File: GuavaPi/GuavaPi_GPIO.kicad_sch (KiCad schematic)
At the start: 1 part

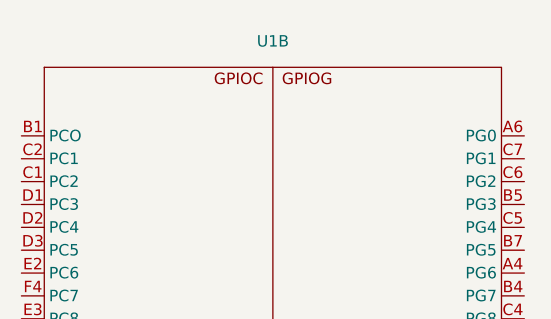
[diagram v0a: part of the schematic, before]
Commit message: Started DRAM Design
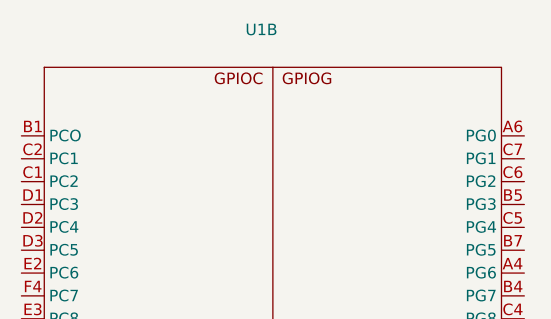
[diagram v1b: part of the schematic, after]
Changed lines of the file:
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@@
   (symbol (lib_id "Allwinner_H616:Allwinner_H616") (at 14.1224 20.828 0) (unit 2)
     (in_bom yes) (on_board yes) (dnp no) (fields_autoplaced)
-    (property "Reference" "U1" (at 52.2224 24.2824 0)
+    (property "Reference" "U1" (at 50.9524 23.0124 0)
       (effects (font (size 1.27 1.27)))
     )
@@
           (reference "U1") (unit 2)
         )
+        (path "/3be7235b-2d12-456d-bbdb-dcc9c2ae1afd/dc1a4d83-a933-4336-ba01-88286996a5dc"
+          (reference "U1") (unit 2)
+        )

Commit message: Added EEMC
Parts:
- added C68, C69, C70, C71, C72, C73: 2u2, symbol Device:C
- added R16, R17: 47k, symbol Device:R
- added U2: EMMC04G-M627-A01, BGA153C50P14X14_1300X1150X100, symbol EMMC04G-M627-A01:EMMC04G-M627-A01
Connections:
- new net: C72.1, C73.1, U2.C2 (VDDI)
- new net +3.3V: C68.2, C69.2, C70.2, C71.2, R16.2, R17.2, U2.C6 (VCCQ), U2.E6 (VCC), U2.F5 (VCC), U2.J10 (VCC), U2.K9 (VCC), U2.M4 (VCCQ), U2.N4 (VCCQ), U2.P3 (VCCQ), U2.P5 (VCCQ)
- new net GND: C68.1, C69.1, C70.1, C71.1, C72.2, C73.2, U2.A6 (VSS), U2.C4 (VSSQ), U2.E7 (VSS), U2.G5 (VSS), U2.H10 (VSS), U2.J5 (VSS), U2.K8 (VSS), U2.N2 (VSSQ), U2.N5 (VSSQ), U2.P4 (VSSQ), U2.P6 (VSSQ)
- new net SDC2_CLK: U2.M6 (CLK)
- new net SDC2_CMD: R16.1, U2.M5 (CMD)
- new net SDC2_D0: U2.A3 (DAT0)
- new net SDC2_D1: U2.A4 (DAT1)
- new net SDC2_D2: U2.A5 (DAT2)
- new net SDC2_D3: U2.B2 (DAT3)
- new net SDC2_D4: U2.B3 (DAT4)
- new net SDC2_D5: U2.B4 (DAT5)
- new net SDC2_D6: U2.B5 (DAT6)
- new net SDC2_D7: U2.B6 (DAT7)
- new net SDC2_DS: R17.1, U2.H5 (DS)
- new net SDC2_RST: U2.K5 (RST_N)

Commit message: WIFI + BT Connections
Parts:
- added A1: RFECA3216060A1T_NEW3_M, picoclick_c3_v1.1:RFECA3216060A1T_NEW3_M, symbol picoclick_c3_v1.1-eagle-import:RFECA3216060A1T_NEW3_M
- added ANT1: 211964-0001, 2119640001:2119640001, symbol 211964-0001:211964-0001
- added B1: BUTTON_4PIN, picoclick_c3_v1.1:BUTTON_SMD_12MM, symbol picoclick_c3_v1.1-eagle-import:BUTTON_4PIN
- added C74, C75: C, symbol Device:C
- added C76: 0.1uF, symbol Device:C
- added C77: 10uF, symbol Device:C
- added C78: 10µ, picoclick_c3_v1.1:C0402_S, symbol picoclick_c3_v1.1-eagle-import:C0402_S
- added C79, C87: 0,1µ, picoclick_c3_v1.1:C0402_S, symbol picoclick_c3_v1.1-eagle-import:C0402_S
- added C80: 2.2uF, symbol Device:C
- added C81, C82: C-EU-0402-WOKEEPOUT_S, picoclick_c3_v1.1:C0402_S, symbol picoclick_c3_v1.1-eagle-import:C-EU-0402-WOKEEPOUT_S
- added C83, C88, C93: 1µ, picoclick_c3_v1.1:C0402_S, symbol picoclick_c3_v1.1-eagle-import:C0402_S
- added C84, C85: 10p, picoclick_c3_v1.1:C0402_S, symbol picoclick_c3_v1.1-eagle-import:C0402_S
- added C86: NC, symbol Device:C
- added C89: C0402_S, picoclick_c3_v1.1:C0402_S, symbol picoclick_c3_v1.1-eagle-import:C0402_S
- added C90: 3.3pF, picoclick_c3_v1.1:C0402_S, symbol picoclick_c3_v1.1-eagle-import:C0402_S
- added C92: 1nH, picoclick_c3_v1.1:C0402_S, symbol picoclick_c3_v1.1-eagle-import:C0402_S
- added D3: DAN222, picoclick_c3_v1.1:SOT523, symbol picoclick_c3_v1.1-eagle-import:DAN222
- added J2: SMT_JUMPER_2_NC_PASTE, picoclick_c3_v1.1:JUMPER_SMALL, symbol picoclick_c3_v1.1-eagle-import:SMT_JUMPER_2_NC_PASTE
- added J4: JUMPER_SMALL, picoclick_c3_v1.1:JUMPER_SMALL, symbol picoclick_c3_v1.1-eagle-import:JUMPER_SMALL
- added R18, R19: R, symbol Device:R
- added R20, R22, R26, R31, R33: 100k, symbol Device:R
- added R21: 0R, symbol Device:R
- added R23: 1k, picoclick_c3_v1.1:R0402, symbol picoclick_c3_v1.1-eagle-import:R0402
- added R24, R25, R28, R29, R30: 10k, picoclick_c3_v1.1:R0402, symbol picoclick_c3_v1.1-eagle-import:R0402
- added R27: 1M, picoclick_c3_v1.1:R0402, symbol picoclick_c3_v1.1-eagle-import:R0402
- added R32, R37, R38, R39, R41, R42: 47k, symbol Device:R
- added R35, R36: 5.1k, picoclick_c3_v1.1:R0402, symbol picoclick_c3_v1.1-eagle-import:R0402
- added U3: ~, symbol Allwinner_H616:6223A-SRD
- added U6: ESP32_C3_QFN32, picoclick_c3_v1.1:QFN32, symbol picoclick_c3_v1.1-eagle-import:ESP32_C3_QFN32
- added U7: MIC5504, picoclick_c3_v1.1:TDFN4, symbol picoclick_c3_v1.1-eagle-import:MIC5504
- added U9: USB_C_C393939, picoclick_c3_v1.1:USBC_C393939, symbol picoclick_c3_v1.1-eagle-import:USB_C_C393939
- added X1: CM9V_T1A, picoclick_c3_v1.1:XTAL_1016, symbol picoclick_c3_v1.1-eagle-import:CM9V_T1A
- added X2: XTAL_2016, picoclick_c3_v1.1:XTAL_2016, symbol picoclick_c3_v1.1-eagle-import:XTAL_2016
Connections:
- net +3.3V: now also R22.2, R32.2
- net GND: now also A1.PGND1 (GND), A1.PGND2 (GND), ANT1.2 (FEED), C74.2, C75.2, C76.2, C77.2, C78.P$1 (1), C79.P$1 (1), C80.1, C81.P$2 (2), C82.P$2 (2), C83.P$1 (1), C84.P$1 (1), C85.P$1 (1), C86.2, C87.P$1 (1), C88.P$1 (1), C89.P$2 (2), C92.P$2 (2), C93.P$1 (1), J2.P$1 (1), R20.1, R24.2, R25.1, R26.2, R27.1, R35.2, R36.2, U3.1 (AGND), U3.20 (AGND), U3.3 (AGND), U3.31 (AGND), U3.33 (AGND), U3.36 (AGND), U6.EXP, U7.EXP (GND), U7.P2 (GND), U9.A1B12 (GND), U9.B1A12 (GND), U9.S1 (SHLD), U9.S2 (SHLD), U9.S3 (SHLD), U9.S4 (SHLD), X2.P2 (G), X2.P4 (G)
- new net: R36.1, U9.B5 (CC2)
- new net: ANT1.1 (GROUND), C75.1, R18.1, R19.1
- new net: C74.1, R18.2, U3.2 (WL_BT_ANT)
- new net: R22.1, U3.34 (BT_DIS#)
- new net: A1.PFEED (ANT), C89.P$1 (1), C90.P$1 (1)
- new net: B1.P2 (2), R23.2
- new net: C76.1, C77.1, R21.2, U3.9 (VBAT_IN)
- new net: R32.1, U3.24 (SUSCLK_IN)
- new net: R35.1, U9.A5 (CC1)
- new net: C84.P$2 (2), U6.30 (XTAL_P), X2.P1 (1)
- new net: C85.P$2 (2), U6.29 (XTAL_N), X2.P3 (2)
- new net: R20.2, U3.6 (HOST_WAKE_BT)
- new net: R31.1, U3.30 (MAIN_XTAL_IN)
- new net +3V3: C78.P$2 (2), C79.P$2 (2), C87.P$2 (2), C93.P$2 (2), R28.1, R29.1, R30.1, U6.11 (VDD3P3_RTC), U6.17 (VDD3P3_CPU), U6.2 (VDD3P3), U6.3 (VDD3P3_1), U6.31 (VDDA), U6.32 (VDDA_1), U7.P1 (VOUT)
- new net +VBAT: B1.P4 (4), C88.P$2 (2), J4.P$1 (1), U7.P4 (VIN)
- new net +VUSB: J4.P$2 (2), U9.A4B9 (VBUS), U9.B4A9 (VBUS)
- new net ADC: U6.9 (MTMS)
- new net AP-CLK24M-OUT: R31.2
- new net AP-SDC1-01: R42.1, U3.19 (SD_D1)
- new net AP-SDC1-CLK: C86.1, U3.17 (SD_CLK)
- new net AP-SDC1-CMD: R39.1, U3.16 (SD_CMD)
- new net AP-SDC1-D0: R41.1, U3.18 (SD_D0)
- new net AP-SDC1-D2: R37.1, U3.14 (SD_D2)
- new net AP-SDC1-D3: R38.1, U3.15 (SD_D3)
- new net AP-UART1-CTS: R26.1, U3.41 (UART_RTS)
- new net AP-UART1-RTS: U3.44 (UART_CTS)
- new net AP-UART1-RX: U3.42 (UART_OUT)
- new net AP-UART1-TX: U3.43 (UART_IN)
- new net BUTTON: C83.P$2 (2), D3.2, R23.1, R24.1, U6.10 (MTDI)
- new net DATA-Ready: U6.19 (SPIHD)
- new net EN: R30.2, U6.7 (CHIP_EN)
- new net EN_LDO: D3.3, R25.2, U7.P3 (EN)
- new net GPIO18: U6.25 (GPIO18), U9.A7 (D-), U9.B7 (D-)
- new net GPIO19: U6.26 (GPIO19), U9.A6 (D+), U9.B6 (D+)
- new net GPIO2: R28.2, U6.6 (GPIO2)
- new net GPIO21: U6.28 (U0TXD)
- new net GPIO8: R29.2, U6.14 (GPIO8)
- new net GPIO9: J2.P$2 (2), U6.15 (GPIO9)
- new net Handshake: U6.8 (GPIO3)
- new net MISO: U6.23 (SPID)
- new net MOSI: U6.24 (SPIQ)
- new net RF_ANT: C90.P$2 (2), C92.P$1 (1), U6.1 (LNA_IN)
- new net SPICLK: U6.22 (SPICLK)
- new net SPISO: U6.21 (SPICS0)
- new net VCC3V3: C80.2, R21.1, R33.2, R37.2, R38.2, R39.2, R41.2, R42.2, U3.22 (VDDIO)
- new net VDD_SPI: D3.1, R27.2, U6.18 (VDD_SPI)
- new net WL-REG-ON: R33.1, U3.12 (WL_DIS#)
- new net WL-WAKE-AP: U3.13 (WL_HOST_WAKE)
- new net X32K_N: C82.P$1 (1), U6.5 (XTAL_32K_N), X1.P$1 (1)
- new net X32K_P: C81.P$1 (1), U6.4 (XTAL_32K_P), X1.P$2 (2)
- no-connect marks 0 -> 14
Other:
- note added: "ANTENNA"
- note added: "C3 ESSENTIALS"
- note added: "Do only close this jumper whithout a battery connected~{}"
- note added: "EMMC"
- note added: "ESP32-C3FN4"
- note added: "POWER LATCH"
- note added: "USB POWERING"
- note added: "USB TYPE-C"
- note added: "VOLTAGE REGULATOR"
- note added: "WIFI + BT"
- moved on the sheet: C68, C69, C70, C71, C72, C73, R16, R17, U1B, U2

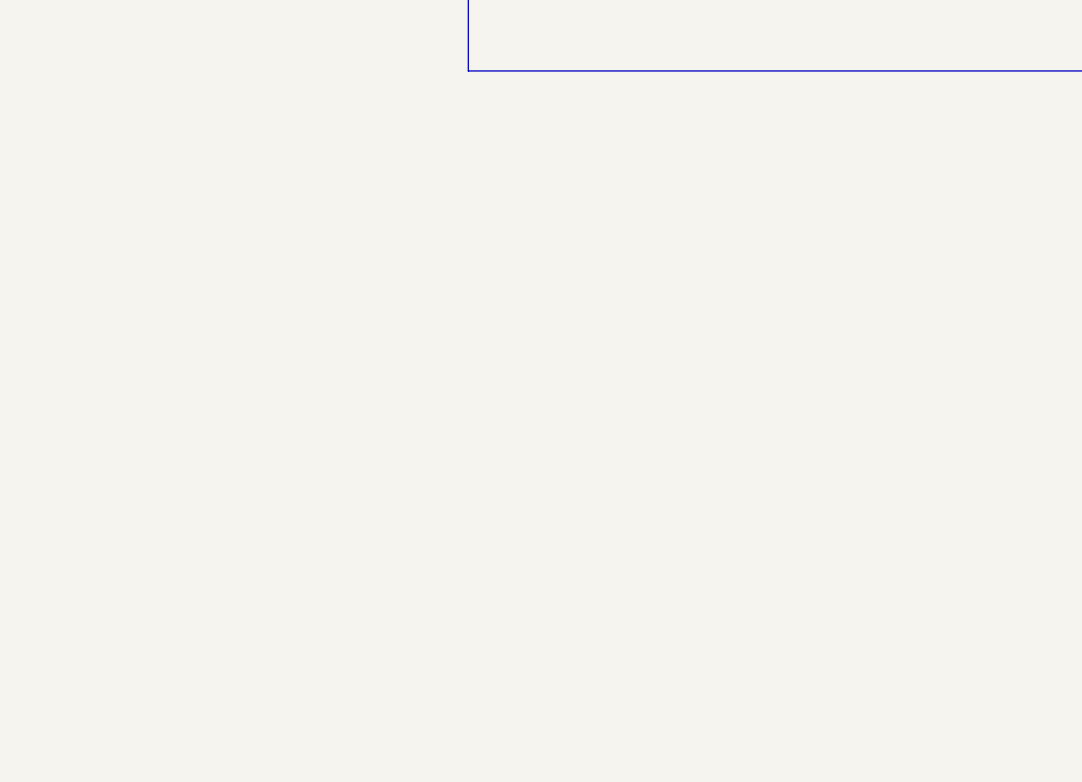
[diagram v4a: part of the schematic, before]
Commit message: SD Card connections
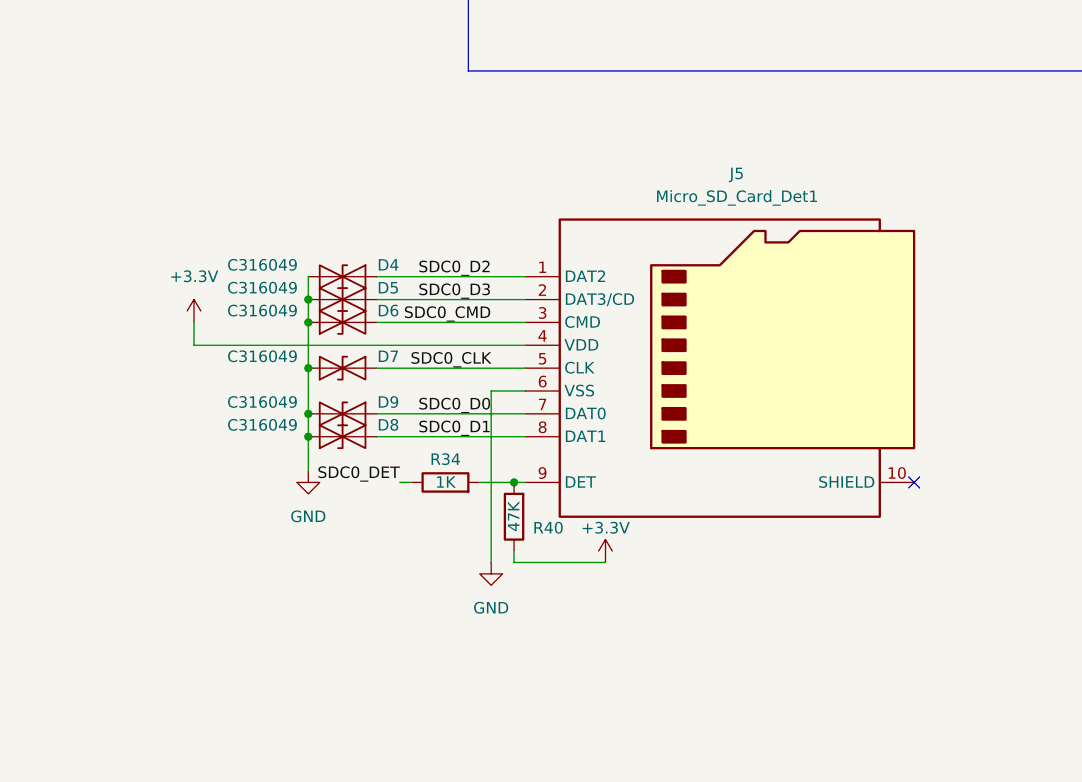
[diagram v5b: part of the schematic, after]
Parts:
- added D4, D5, D6, D7, D8, D9: C316049, Diode_SMD:D_SOD-323, symbol Diode:SD05_SOD323
- added J5: Micro_SD_Card_Det1, symbol Connector:Micro_SD_Card_Det1
- added R34: 1K, symbol Device:R
- added R40: 47K, symbol Device:R
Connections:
- net +3.3V: now also J5.4 (VDD), R40.1
- net GND: now also D4.1 (A1), D5.1 (A1), D6.1 (A1), D7.1 (A1), D8.1 (A1), D8.2 (A2), D9.1 (A1), D9.2 (A2), J5.6 (VSS), J5.7 (DAT0), J5.8 (DAT1)
- new net: J5.9 (DET), R34.2, R40.2
- new net SDC0_CLK: D7.2 (A2), J5.5 (CLK)
- new net SDC0_CMD: D6.2 (A2), J5.3 (CMD)
- new net SDC0_D2: D4.2 (A2), J5.1 (DAT2)
- new net SDC0_D3: D5.2 (A2), J5.2 (DAT3/CD)
- new net SDC0_DET: R34.1
- no-connect marks 14 -> 15

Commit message: SPI Flash
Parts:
- removed D4, D5, D6, D7, D8, D9: C316049, Diode_SMD:D_SOD-323, symbol Diode:SD05_SOD323
- removed R40: 47K, symbol Device:R
- added C97: 0.1uF, symbol Device:C
- added R13: 10K, symbol Device:R
- added R43: 33R, symbol Device:R
- R34: value 1K -> 10K
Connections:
- net AP-SDC1-01 is gone; now on net AP-SDC1-D1: R42.1, U3.19 (SD_D1)
- net +3.3V: no longer J5.4 (VDD)
- net AP-SDC1-CLK: now also U1.A6 (PG0/SDC1_CLK/PG_EINT0)
- net AP-SDC1-CMD: now also U1.C7 (PG1/SDC1_CMD/PG_EINT1)
- net AP-SDC1-D0: now also U1.C6 (PG2/SDC1_D0/PG_EINT2)
- net AP-SDC1-D2: now also U1.C5 (PG4/SDC1_D2/PG_EINT4)
- net AP-SDC1-D3: now also U1.B7 (PG5/SDC1_D3/PG_EINT5)
- net AP-UART1-CTS: now also U1.B3 (PG9/UART1_CTS/JTAG_DI/AC_ADCY/PG_EINT9)
- net AP-UART1-RTS: now also U1.C4 (PG8/UART1_RTS/PLL_LOCK_DBG/JTAG_DO/PG_EINT8)
- net AP-UART1-RX: now also U1.B4 (PG7/UART1_RX/JTAG_CK/PG_EINT7)
- net AP-UART1-TX: now also U1.A4 (PG6/UART1_TX/JTAG_MS/PG_EINT6)
- net GND: now also U1.J2 (PF0), U1.J3 (PF1), C97.1
- net SDC0_CLK: now also R43.1
- net SDC0_CMD: now also U1.K3 (PF3), R13.2
- net SDC0_D2: now also U1.L3 (PF5)
- net SDC0_D3: now also U1.L2 (PF4)
- net SDC0_DET: now also J5.9 (DET), R34.2, U1.K2 (PF6); no longer R34.1
- net VCC3V3: now also J5.4 (VDD), R34.1, U1.D7 (VCC_PG), C97.2, R13.1
- net WL-REG-ON: now also U1.A2 (PG18)
- net WL-WAKE-AP: now also U1.A8 (PG15)
- net BT-RESETN: now reaches R22.1, U3.34 (BT_DIS#)
- net BT-RESETN: now also U1.B2 (PG19)
- net AP-WAKE-BT: now reaches R20.2, U3.6 (HOST_WAKE_BT)
- net AP-WAKE-BT: now also U1.C3 (PG17)
- net SPI1-MOSI: now reaches U1.B12 (PH7/UART2_RTS/H_I2S3_LRCK/SPI1_MOSI)
- net SPI1-CSO: now reaches U1.B14 (PH5/UART2_TX/H_I2S3_MCLK/SPI1_CS0)
- net TX5: now reaches U1.B15 (PH2)
- net AP-SDC1-D1: now reaches U1.B5 (PG3/SDC1_D1/PG_EINT3)
- net BT-WAKE-AP: now reaches U1.B8 (PG16)
- net BT-WAKE-AP: now also U3.7 (BT_WAKE_HOST)
- net SPI0-MOSI: now reaches U1.C1 (PC2)
- net SPI1-MISO: now reaches U1.C13 (PH8/UART2_CTS/H_I2S3_DOUT0/SPI1_MISO/H_I2S3_DIN1)
- net SPI1-CLK: now reaches U1.C14 (PH6/UART2_RX/H_I2S3_BCLK/SPI1_CLK)
- net RX5: now reaches U1.C15 (PH3)
- net SPI0-CS0: now reaches U1.D1 (PC3)
- net RX0: now reaches U1.D15 (PH1)
- net TX0: now reaches U1.D16 (PHO)
- net SPI0-MISO: now reaches U1.D2 (PC4)
- net SEL3: now reaches U1.D3 (PC5)
- net SEL4: now reaches U1.E2 (PC6)
- net at U1.K1 (PF2): now also R43.2
- no-connect marks 15 -> 22
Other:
- note added: "D7 -> H3"
- note added: "NC FLASH"
- note added: "SDCARD"
- note added: "UART & SPI1"
- note added: "WIFI+BT"
- moved on the sheet: C68, C69, C70, C71, C72, C73, J5, R16, R17, R34, U2
